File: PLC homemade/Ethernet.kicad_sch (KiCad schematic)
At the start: 36 parts, among them J7 SS-74810-004, U3 W5500, Y1 Crystal

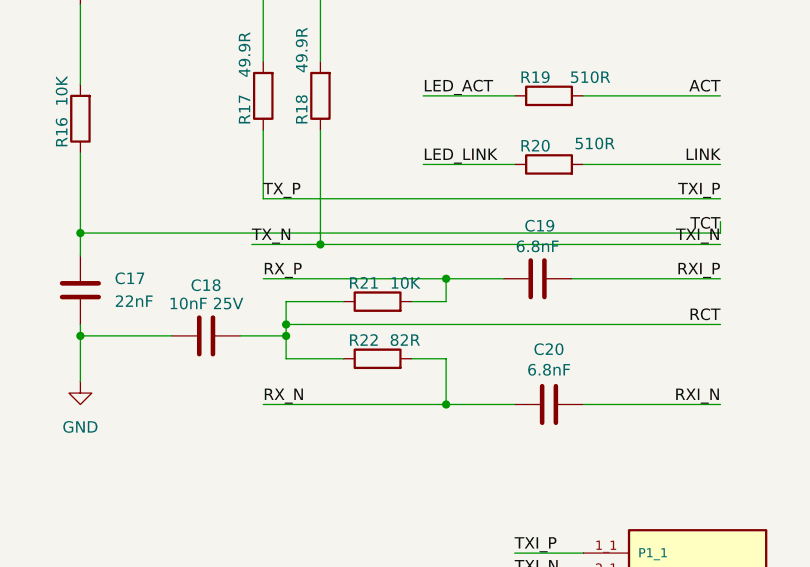
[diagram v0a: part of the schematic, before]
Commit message: :ambulance:2output and usbc
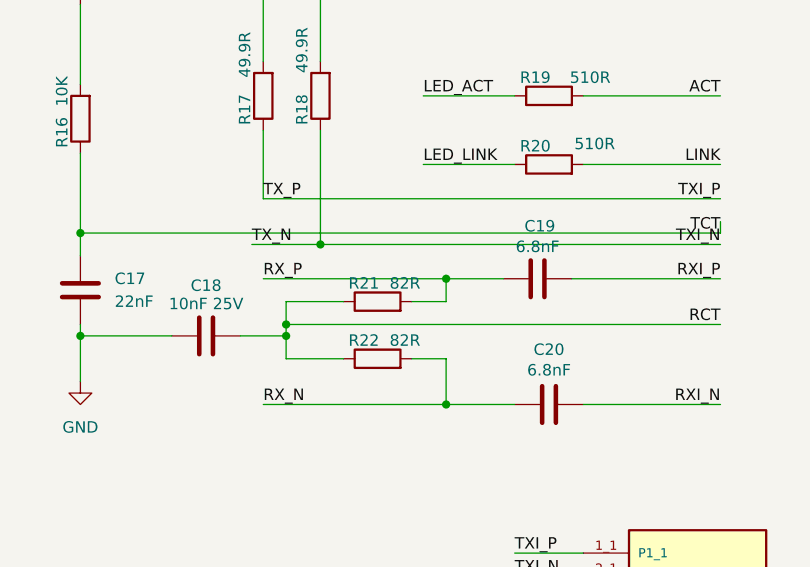
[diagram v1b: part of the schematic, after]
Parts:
- R21: value 10K -> 82R
- R22: footprint Resistor_SMD:R_1206_3216Metric -> Resistor_SMD:R_01005_0402Metric
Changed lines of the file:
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@@
 			)
 		)
-		(property "Footprint" "Resistor_SMD:R_1206_3216Metric"
+		(property "Footprint" "Resistor_SMD:R_01005_0402Metric"
 			(at 170.18 81.788 90)
 			(effects
@@
 			)
 		)
-		(property "Value" "10K"
+		(property "Value" "82R"
 			(at 173.228 71.628 90)
 			(effects
